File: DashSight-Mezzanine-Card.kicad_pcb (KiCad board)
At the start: 2 copper layers, 75.1 x 77.5 mm, 71 parts, among them IC1 XM1110, IC2 ELM327, J1 Pi2 Connector, J2 Euler Connector, J3 Conn_Coaxial, J4 OBD2-DB9_Male, Q1 2N3904, Q2 2N3906, Q3 2N3906, Q4 2N3904, Q5 2N3904, Q6 2N3904, Q7 2N3904, U1 MCP2561-E/P, U2 LM317L_TO92, U3 LP2950-3.0_TO92, U4 ADuM1201AR, Y1 4.0MHz

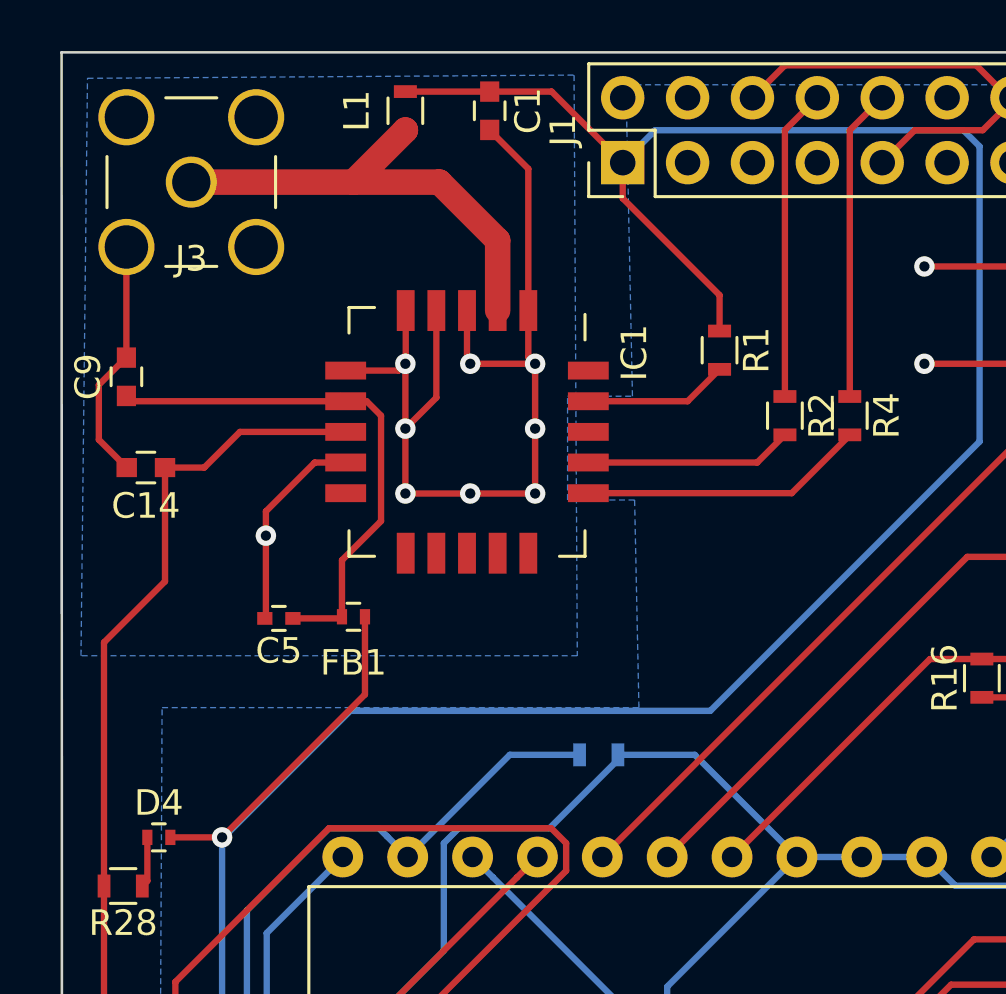
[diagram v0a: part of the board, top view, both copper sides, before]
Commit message: PCB: Reduce antenna distance and regenerate production files
Signed-off-by: Alistair Francis <alistair@alistair23.me>
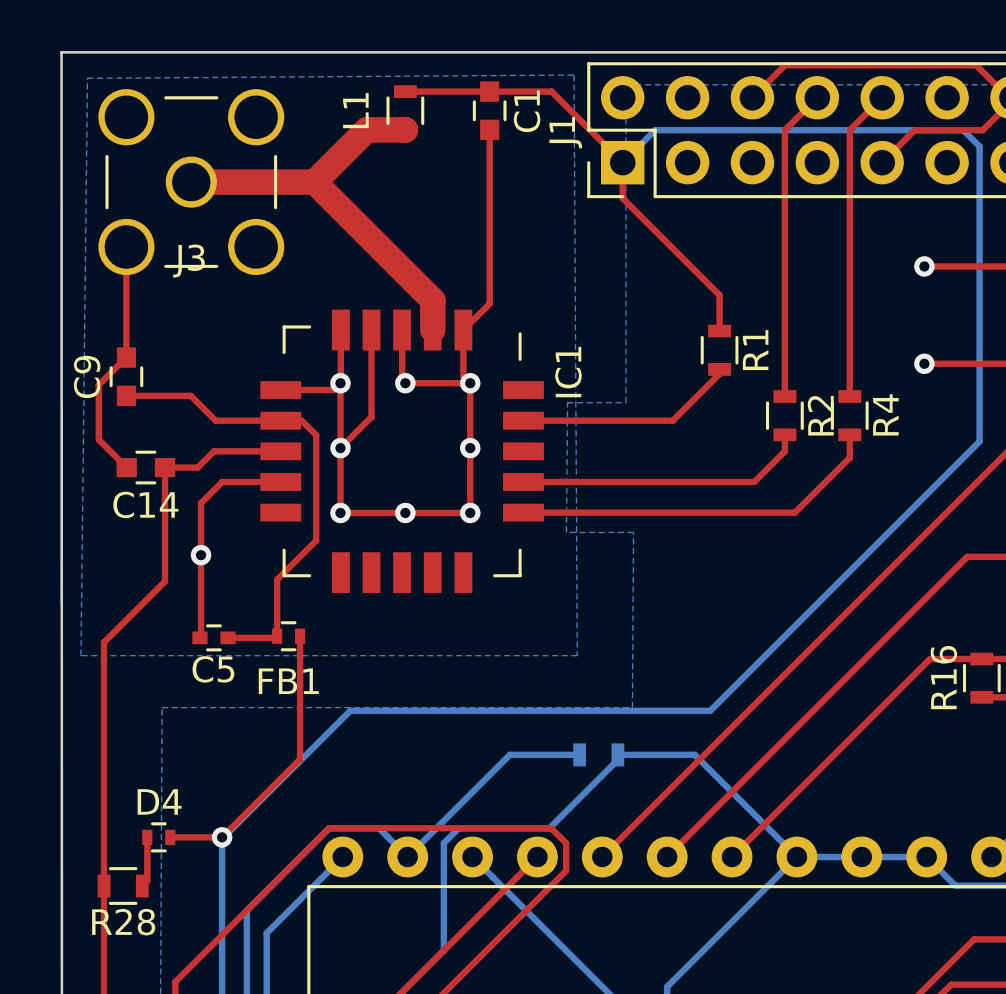
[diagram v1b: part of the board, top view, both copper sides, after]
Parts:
- moved C5 2.65 mm to (130.9, 70.4)
- moved FB1 2.65 mm to (133.9, 70.4)
- moved IC1 2.65 mm to (138.3, 63.1)
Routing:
- net Net-(IC1-Pad16): track 11.2 -> 14.6 mm
- net Net-(IC1-Pad17): track 8.15 -> 11.4 mm
- net Net-(IC1-Pad19): track 5.65 -> 8.62 mm
- net Net-(BT1-Pad1): track 76.2 -> 73.4 mm
- net Net-(C5-Pad1): track 21.7 -> 19.8 mm
- net +3V3: track 151.1 -> 149.3 mm
- net Net-(IC1-Pad2): track 18.6 -> 16.9 mm
- net GND: track 343.6 -> 344.8 mm

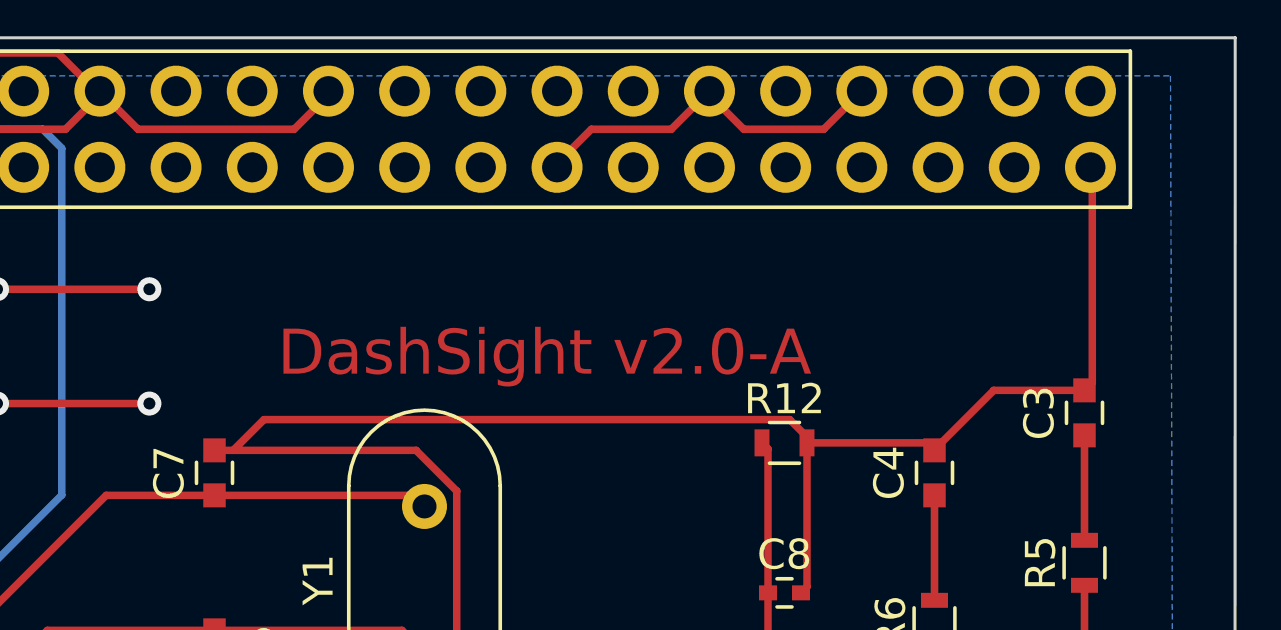
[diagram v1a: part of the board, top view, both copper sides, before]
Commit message: kicad_pcb: Add OSH logo and regenerate PCB-Fab
Signed-off-by: Alistair Francis <alistair@alistair23.me>
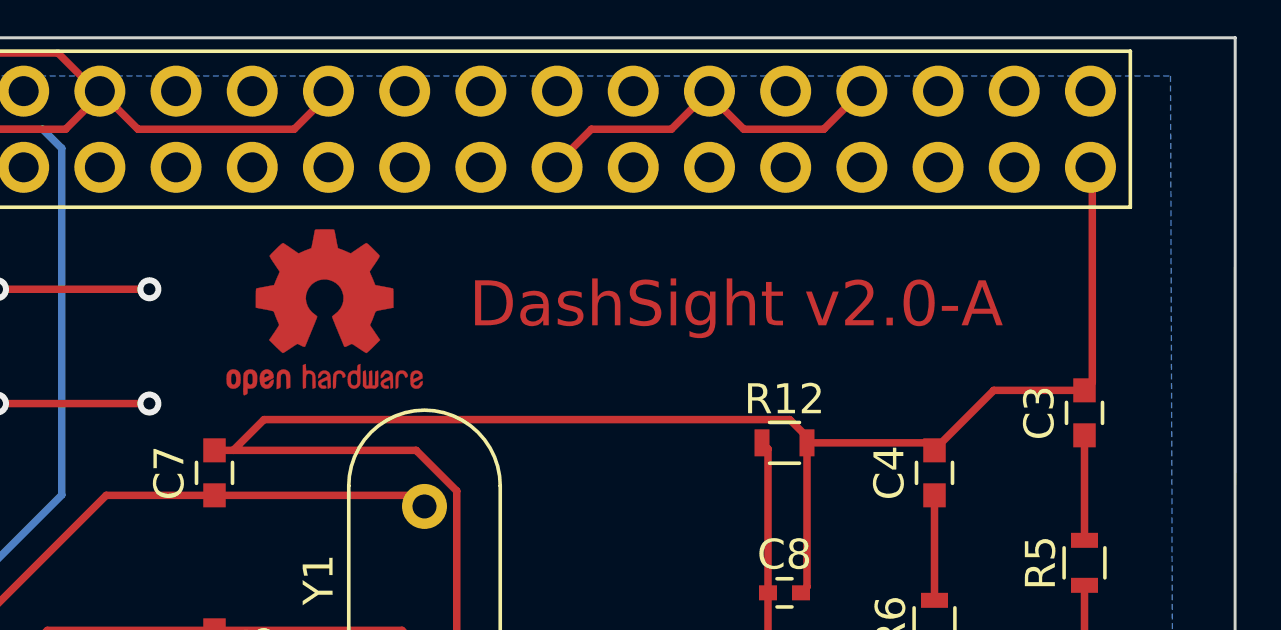
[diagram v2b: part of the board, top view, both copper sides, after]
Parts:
- added REF***: OSHW-Logo2_7.3x6mm_Copper, Symbols:OSHW-Logo2_7.3x6mm_Copper, F.Cu at (169.7, 56.6)

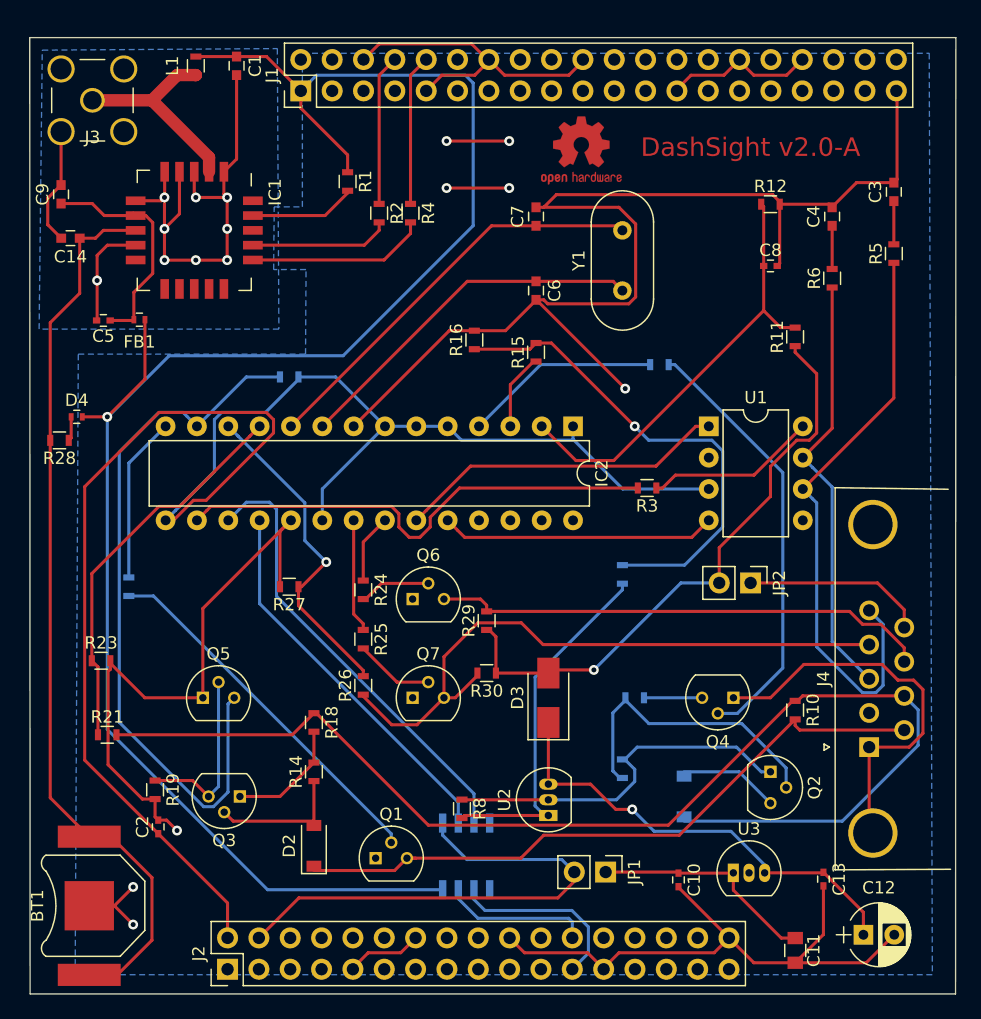
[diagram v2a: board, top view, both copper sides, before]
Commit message: sch: Update the OBD2 voltage regulator
Signed-off-by: Alistair Francis <alistair@alistair23.me>
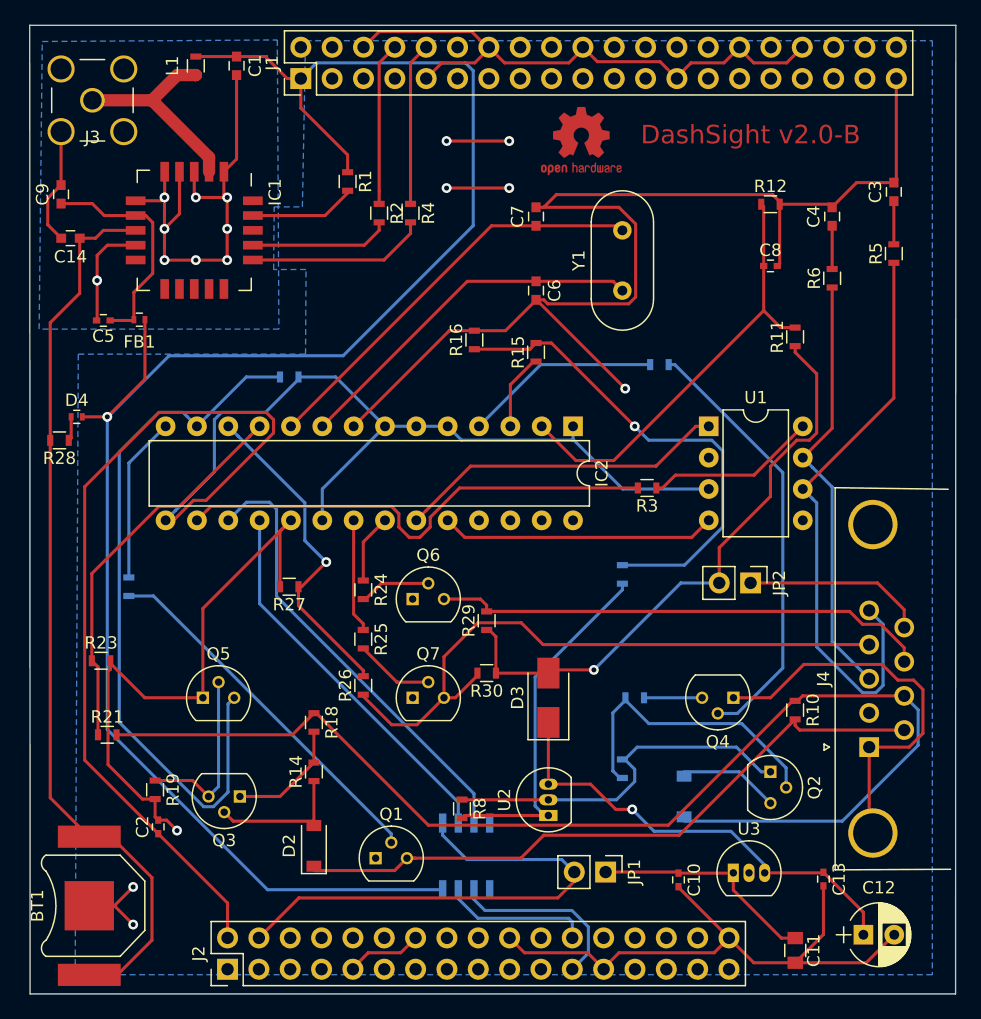
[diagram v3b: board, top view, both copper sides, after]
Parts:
- moved J1 1.00 mm to (146.9, 50.8)
- moved REF*** 0.76 mm to (169.7, 55.9)
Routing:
- net GND: track 344.8 -> 354.9 mm
- net +3V3: track 149.3 -> 150.9 mm
- net UART2_TX: track 12.6 -> 13.6 mm
- net UART2_RX: track 12.2 -> 13.2 mm
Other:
- board size 75.1 x 77.5 mm -> 75.1 x 78.5 mm
- board text added: "DashSight v2.0-B"
- board text removed: "DashSight v2.0-A"

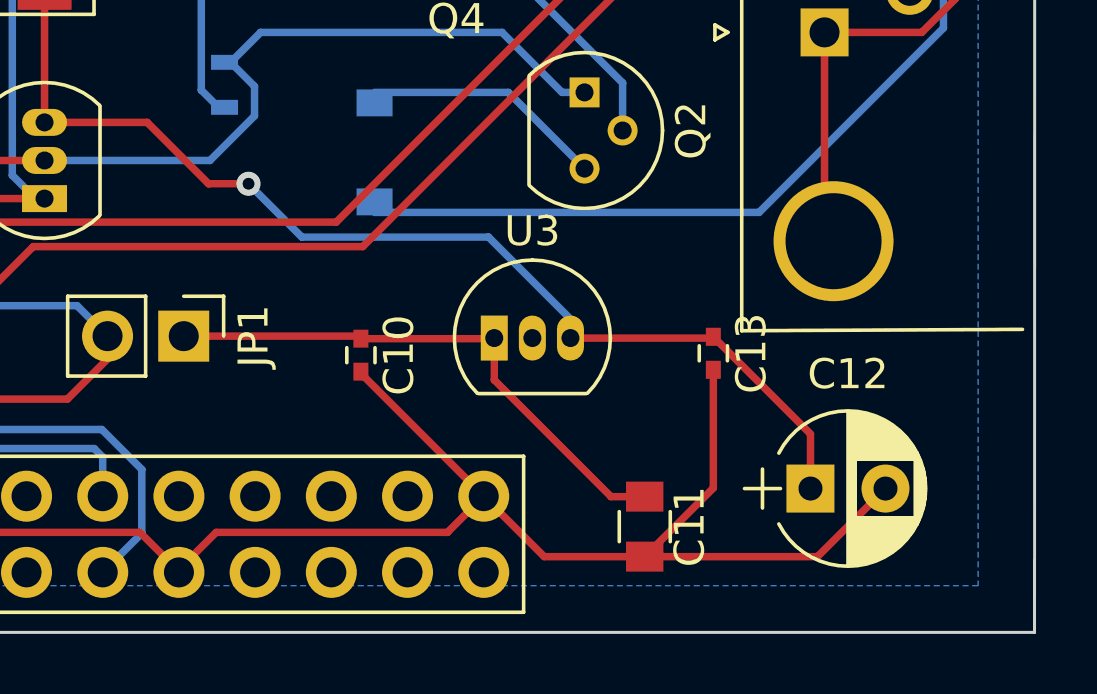
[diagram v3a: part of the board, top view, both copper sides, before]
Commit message: pcb: Replace with the new voltage regulator
Signed-off-by: Alistair Francis <alistair@alistair23.me>
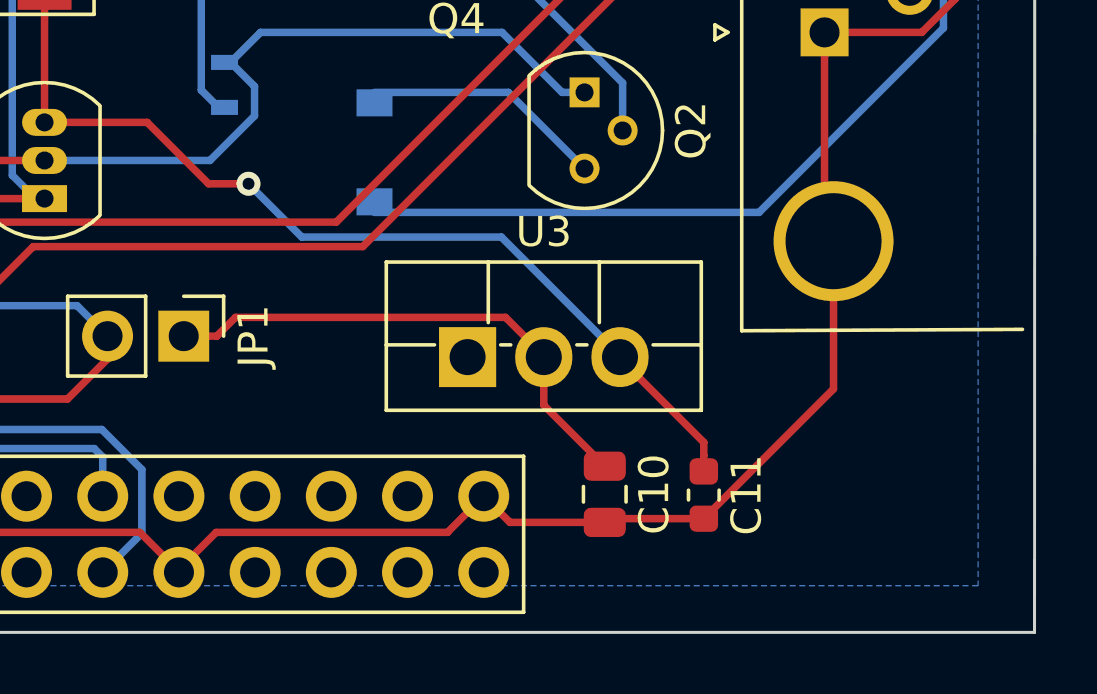
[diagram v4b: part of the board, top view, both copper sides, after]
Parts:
- removed C12: 2.2uF 50V, Capacitors_THT:CP_Radial_D5.0mm_P2.50mm
- removed C13: 0.1uF 50V, Capacitors_SMD:C_0402
- C10: value 0.1uF -> 10uF 10V; footprint Capacitors_SMD:C_0402 -> Capacitor_SMD:C_0805_2012Metric
- C11: value 4.7uF 10V -> 10uF; footprint Capacitors_SMD:C_0805 -> Capacitor_SMD:C_0603_1608Metric
- U3: value LP2950-3.0_TO92 -> LM1085-5.0; footprint TO_SOT_Packages_THT:TO-92_Inline_Narrow_Oval -> Package_TO_SOT_THT:TO-220F-3_Vertical
- moved C10 9.36 mm to (185.7, 120.4)
- moved C11 2.23 mm to (189.0, 120.4)
- moved U3 1.09 mm to (181.1, 115.8)
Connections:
- C11 pad 1: Net-(C10-Pad1) -> V12
- U3 pad 1: Net-(C10-Pad1) -> GND
- U3 pad 2: GND -> Net-(C10-Pad1)
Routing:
- net GND: track 354.9 -> 345.5 mm
- net V12: track 37.1 -> 32.4 mm
- net Net-(C10-Pad1): track 18.4 -> 17.3 mm
